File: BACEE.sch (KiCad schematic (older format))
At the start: 13 parts, among them U1 24LC1025, U2 DS1337S+, U3 24LC1025, U4 ATMEGA328P-AU, Y1 Crystal32768KHz, Y2 Crystal 16MHz

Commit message: Adjusted designators, units etc as per Larry's feedback.
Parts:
- removed C3: 10uF, Capacitor_SMD:C_0805_2012Metric_Pad1.15x1.40mm_HandSolder, symbol Device:CP1
- added C3: 10 uF, Capacitor_SMD:C_0805_2012Metric_Pad1.15x1.40mm_HandSolder, symbol Device:CP
- C1, C2: value 22pF -> 22 pF
- R1: value 330Ohm -> 330 Ω
- R2: value 10kOhm -> 10 kΩ
- Y1: value Crystal32768KHz -> Crystal 32768 kHz
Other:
- note added: "N1 - Clock/Calendar"
- note added: "N2 - Atmega328P-PU with oscillator and battery"
- note added: "N3 - EEPROM"
- note added: "N4 - Connectors sheet"
- note removed: "Atmega328P-PU with oscillator and battery"
- note removed: "Clock/Calendar"
- note removed: "Connectors sheet"
- note removed: "EEPROM"
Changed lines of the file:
@@
 EESchema Schematic File Version 4
+LIBS:BACEE-cache
 EELAYER 26 0
 EELAYER END
@@
 P 6150 1950
 F 0 "C1" V 5898 1950 50  0000 C CNN
-F 1 "22pF" V 5989 1950 50  0000 C CNN
+F 1 "22 pF" V 5989 1950 50  0000 C CNN
 F 2 "Capacitor_SMD:C_0805_2012Metric_Pad1.15x1.40mm_HandSolder" H 6188 1800 50  0001 C CNN
 F 3 "~" H 6150 1950 50  0001 C CNN
@@
 P 6150 2500
 F 0 "C2" V 5898 2500 50  0000 C CNN
-F 1 "22pF" V 5989 2500 50  0000 C CNN
+F 1 "22 pF" V 5989 2500 50  0000 C CNN
 F 2 "Capacitor_SMD:C_0805_2012Metric_Pad1.15x1.40mm_HandSolder" H 6188 2350 50  0001 C CNN
 F 3 "~" H 6150 2500 50  0001 C CNN
@@
 $EndComp
 $Comp
-L Device:CP1 C3
-U 1 1 5B7FD83B
-P 9450 2650
-F 0 "C3" H 9565 2696 50  0000 L CNN
-F 1 "10uF" H 9565 2605 50  0000 L CNN
-F 2 "Capacitor_SMD:C_0805_2012Metric_Pad1.15x1.40mm_HandSolder" H 9450 2650 50  0001 C CNN
-F 3 "~" H 9450 2650 50  0001 C CNN
-	1    9450 2650
-	1    0    0    -1
-$EndComp
-$Comp
 L Device:R R1
 U 1 1 5B7FD90B
 P 6100 3600
 F 0 "R1" H 6030 3554 50  0000 R CNN
-F 1 "330Ohm" H 6030 3645 50  0000 R CNN
+F 1 "330 Ω" H 6030 3645 50  0000 R CNN
 F 2 "Resistor_SMD:R_0805_2012Metric_Pad1.15x1.40mm_HandSolder" V 6030 3600 50  0001 C CNN
 F 3 "~" H 6100 3600 50  0001 C CNN
@@
 P 6900 4150
 F 0 "R2" H 6970 4196 50  0000 L CNN
-F 1 "10kOhm" H 6970 4105 50  0000 L CNN
+F 1 "10 kΩ" H 6970 4105 50  0000 L CNN
 F 2 "Resistor_SMD:R_0805_2012Metric_Pad1.15x1.40mm_HandSolder" V 6830 4150 50  0001 C CNN
 F 3 "~" H 6900 4150 50  0001 C CNN
@@
 P 2700 1650
 F 0 "Y1" V 2746 1519 50  0000 R CNN
-F 1 "Crystal32768KHz" V 2655 1519 50  0000 R CNN
+F 1 "Crystal 32768 kHz" V 2655 1519 50  0000 R CNN
 F 2 "Crystal:Crystal_SMD_MicroCrystal_CC7V-T1A-2Pin_3.2x1.5mm_HandSoldering" H 2700 1650 50  0001 C CNN
 F 3 "~" H 2700 1650 50  0001 C CNN
@@
 Wire Notes Line
 	10750 5200 10750 950
-Text Notes 7150 900  2    50   ~ 0
-Atmega328P-PU with oscillator and battery
+Text Notes 7375 925  2    50   ~ 0
+N2 - Atmega328P-PU with oscillator and battery
 Wire Notes Line
 	2500 950  2500 2800
@@
 Wire Notes Line
 	5300 3000 2500 3000
-Text Notes 3100 900  2    50   ~ 0
-Clock/Calendar
-Text Notes 2800 2950 2    50   ~ 0
-EEPROM
+Text Notes 3325 925  2    50   ~ 0
+N1 - Clock/Calendar
+Text Notes 3025 3000 2    50   ~ 0
+N3 - EEPROM
 Wire Notes Line
 	2500 4650 2500 6200
@@
 Wire Notes Line
 	5300 4650 2500 4650
-Text Notes 3150 4600 2    50   ~ 0
-Connectors sheet
+Text Notes 3375 4650 2    50   ~ 0
+N4 - Connectors sheet
+$Comp
+L Device:CP C3
+U 1 1 5BA040EC
+P 9450 2650
+F 0 "C3" H 9568 2696 50  0000 L CNN
+F 1 "10 uF" H 9568 2605 50  0000 L CNN
+F 2 "Capacitor_SMD:C_0805_2012Metric_Pad1.15x1.40mm_HandSolder" H 9488 2500 50  0001 C CNN
+F 3 "~" H 9450 2650 50  0001 C CNN
+	1    9450 2650
+	1    0    0    -1
+$EndComp
 $EndSCHEMATC

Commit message: Adjusted designators, units etc as per Larry's feedback.
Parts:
- renumbered D1 to DS1
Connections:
- net labels added: GNDPWR
- net labels removed: GND
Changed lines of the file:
@@
 $EndComp
 $Comp
-L Device:LED D1
+L Device:LED DS1
 U 1 1 5B7FDA0F
 P 6750 3200
-F 0 "D1" H 6741 3416 50  0000 C CNN
+F 0 "DS1" H 6741 3416 50  0000 C CNN
 F 1 "LED" H 6741 3325 50  0000 C CNN
 F 2 "LED_SMD:LED_0805_2012Metric_Pad1.15x1.40mm_HandSolder" H 6750 3200 50  0001 C CNN
@@
 F 3 "~" V 10000 2710 50  0001 C CNN
 	1    10000 2650
-	1    0    0    -1
-$EndComp
-$Comp
-L power:GND #PWR02
-U 1 1 5B7FDCEB
-P 10000 3250
-F 0 "#PWR02" H 10000 3000 50  0001 C CNN
-F 1 "GND" H 10005 3077 50  0000 C CNN
-F 2 "" H 10000 3250 50  0001 C CNN
-F 3 "" H 10000 3250 50  0001 C CNN
-	1    10000 3250
 	1    0    0    -1
 $EndComp
@@
 F17 "TX" O L 3550 5400 50
 $EndSheet
-$Comp
-L power:GND #PWR01
-U 1 1 5B7FEA2F
-P 2950 5150
-F 0 "#PWR01" H 2950 4900 50  0001 C CNN
-F 1 "GND" H 2955 4977 50  0000 C CNN
-F 2 "" H 2950 5150 50  0001 C CNN
-F 3 "" H 2950 5150 50  0001 C CNN
-	1    2950 5150
-	1    0    0    -1
-$EndComp
 Text Label 3450 5050 2    50   ~ 0
 Vcc
@@
 Wire Wire Line
 	6750 2500 6750 2350
-$Comp
-L power:GND #PWR0101
-U 1 1 5B805229
-P 5750 2650
-F 0 "#PWR0101" H 5750 2400 50  0001 C CNN
-F 1 "GND" H 5755 2477 50  0000 C CNN
-F 2 "" H 5750 2650 50  0001 C CNN
-F 3 "" H 5750 2650 50  0001 C CNN
-	1    5750 2650
-	1    0    0    -1
-$EndComp
 Wire Wire Line
 	6750 1950 6300 1950
@@
 Wire Wire Line
 	6100 3200 6100 3450
-$Comp
-L power:GND #PWR0102
-U 1 1 5B806E4B
-P 6100 3950
-F 0 "#PWR0102" H 6100 3700 50  0001 C CNN
-F 1 "GND" H 6105 3777 50  0000 C CNN
-F 2 "" H 6100 3950 50  0001 C CNN
-F 3 "" H 6100 3950 50  0001 C CNN
-	1    6100 3950
-	1    0    0    -1
-$EndComp
 Wire Wire Line
 	6100 3750 6100 3950
@@
 NoConn ~ 7650 4300
 NoConn ~ 7650 4500
-$Comp
-L power:GND #PWR0103
-U 1 1 5B811509
-P 8250 4950
-F 0 "#PWR0103" H 8250 4700 50  0001 C CNN
-F 1 "GND" H 8255 4777 50  0000 C CNN
-F 2 "" H 8250 4950 50  0001 C CNN
-F 3 "" H 8250 4950 50  0001 C CNN
-	1    8250 4950
-	1    0    0    -1
-$EndComp
 Wire Wire Line
 	8150 4800 8150 4900
@@
 Text Label 4300 3700 2    50   ~ 0
 ADDS2
-$Comp
-L power:GND #PWR0104
-U 1 1 5B8142A1
-P 4100 2450
-F 0 "#PWR0104" H 4100 2200 50  0001 C CNN
-F 1 "GND" H 4105 2277 50  0000 C CNN
-F 2 "" H 4100 2450 50  0001 C CNN
-F 3 "" H 4100 2450 50  0001 C CNN
-	1    4100 2450
-	1    0    0    -1
-$EndComp
 Wire Wire Line
 	4100 2200 4100 2450
@@
 Wire Wire Line
 	4700 4150 4700 4000
-$Comp
-L power:GND #PWR0105
-U 1 1 5B81A59B
-P 3950 4250
-F 0 "#PWR0105" H 3950 4000 50  0001 C CNN
-F 1 "GND" H 3955 4077 50  0000 C CNN
-F 2 "" H 3950 4250 50  0001 C CNN
-F 3 "" H 3950 4250 50  0001 C CNN
-	1    3950 4250
-	1    0    0    -1
-$EndComp
 Wire Wire Line
 	3950 4250 3950 4150
@@
 	1    0    0    -1
 $EndComp
+$Comp
+L power:GNDPWR #PWR0101
+U 1 1 5BA085A3
+P 5750 2650
+F 0 "#PWR0101" H 5750 2450 50  0001 C CNN
+F 1 "GNDPWR" H 5754 2496 50  0000 C CNN
+F 2 "" H 5750 2600 50  0001 C CNN
+F 3 "" H 5750 2600 50  0001 C CNN
+	1    5750 2650
+	1    0    0    -1
+$EndComp
+$Comp
+L power:GNDPWR #PWR0102
+U 1 1 5BA08918
+P 4100 2450
+F 0 "#PWR0102" H 4100 2250 50  0001 C CNN
+F 1 "GNDPWR" H 4104 2296 50  0000 C CNN
+F 2 "" H 4100 2400 50  0001 C CNN
+F 3 "" H 4100 2400 50  0001 C CNN
+	1    4100 2450
+	1    0    0    -1
+$EndComp
+$Comp
+L power:GNDPWR #PWR0103
+U 1 1 5BA08A66
+P 3950 4250
+F 0 "#PWR0103" H 3950 4050 50  0001 C CNN
+F 1 "GNDPWR" H 3954 4096 50  0000 C CNN
+F 2 "" H 3950 4200 50  0001 C CNN
+F 3 "" H 3950 4200 50  0001 C CNN
+	1    3950 4250
+	1    0    0    -1
+$EndComp
+$Comp
+L power:GNDPWR #PWR0104
+U 1 1 5BA08BE8
+P 6100 3950
+F 0 "#PWR0104" H 6100 3750 50  0001 C CNN
+F 1 "GNDPWR" H 6104 3796 50  0000 C CNN
+F 2 "" H 6100 3900 50  0001 C CNN
+F 3 "" H 6100 3900 50  0001 C CNN
+	1    6100 3950
+	1    0    0    -1
+$EndComp
+$Comp
+L power:GNDPWR #PWR0105
+U 1 1 5BA08E06
+P 2950 5150
+F 0 "#PWR0105" H 2950 4950 50  0001 C CNN
+F 1 "GNDPWR" H 2954 4996 50  0000 C CNN
+F 2 "" H 2950 5100 50  0001 C CNN
+F 3 "" H 2950 5100 50  0001 C CNN
+	1    2950 5150
+	1    0    0    -1
+$EndComp
+$Comp
+L power:GNDPWR #PWR0106
+U 1 1 5BA0915C
+P 8250 4950
+F 0 "#PWR0106" H 8250 4750 50  0001 C CNN
+F 1 "GNDPWR" H 8254 4796 50  0000 C CNN
+F 2 "" H 8250 4900 50  0001 C CNN
+F 3 "" H 8250 4900 50  0001 C CNN
+	1    8250 4950
+	1    0    0    -1
+$EndComp
+$Comp
+L power:GNDPWR #PWR0107
+U 1 1 5BA091C0
+P 10000 3250
+F 0 "#PWR0107" H 10000 3050 50  0001 C CNN
+F 1 "GNDPWR" H 10004 3096 50  0000 C CNN
+F 2 "" H 10000 3200 50  0001 C CNN
+F 3 "" H 10000 3200 50  0001 C CNN
+	1    10000 3250
+	1    0    0    -1
+$EndComp

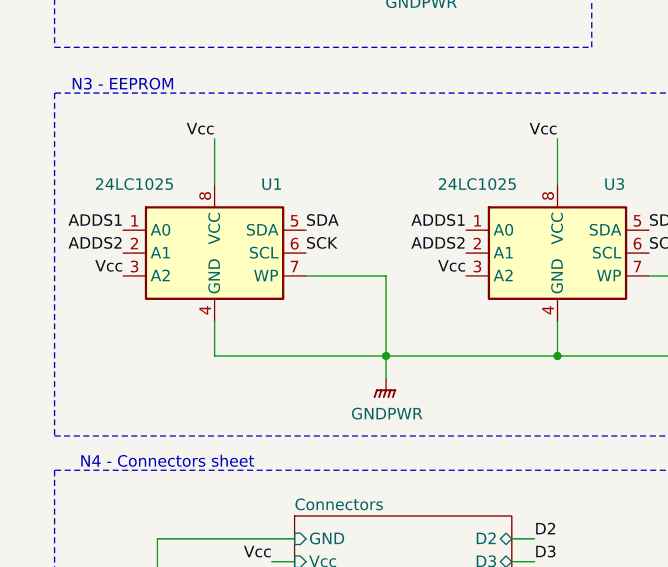
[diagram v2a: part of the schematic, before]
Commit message: Corrected error in addressing pins of EEPROM modules.
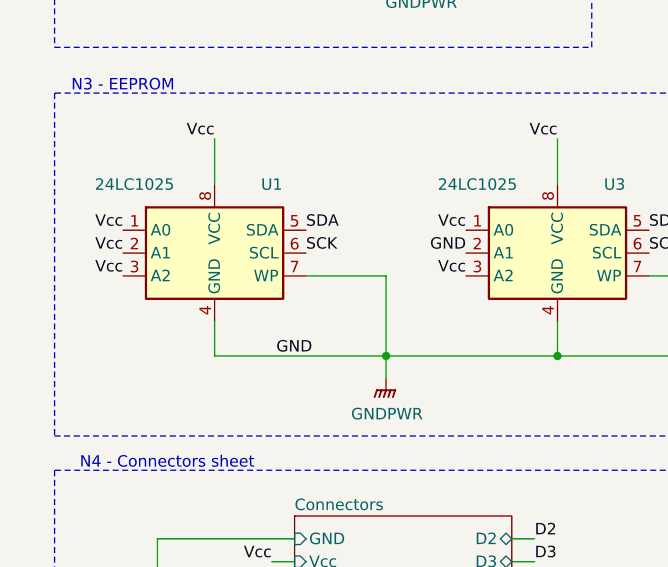
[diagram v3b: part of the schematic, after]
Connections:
- net ADDS1: no longer U1.1 (A0), U3.1 (A0)
- net ADDS2: no longer U1.2 (A1), U3.2 (A1)
- net GNDPWR: now also U3.2 (A1)
- net Vcc: now also U1.1 (A0), U1.2 (A1), U3.1 (A0)
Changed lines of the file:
@@
 Text Label 5100 3600 0    50   ~ 0
 SDA
-Text Label 2800 3600 2    50   ~ 0
-ADDS1
-Text Label 4300 3600 2    50   ~ 0
-ADDS1
-Text Label 2800 3700 2    50   ~ 0
-ADDS2
-Text Label 4300 3700 2    50   ~ 0
-ADDS2
 Wire Wire Line
 	4100 2200 4100 2450
@@
 	1    0    0    -1
 $EndComp
+Text Label 3470 4150 0    50   ~ 0
+GND
+Text Label 2800 3600 2    50   ~ 0
+Vcc
+Text Label 2800 3700 2    50   ~ 0
+Vcc
+Text Label 4300 3600 2    50   ~ 0
+Vcc
+Text Label 4300 3700 2    50   ~ 0
+GND
 $EndSCHEMATC
